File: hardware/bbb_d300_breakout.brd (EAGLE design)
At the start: 68 x 54.5 mm, 10 parts, among them SW1 JTP1236, X1 STEPCRAFT, X2 RJ45, X3 RJ45

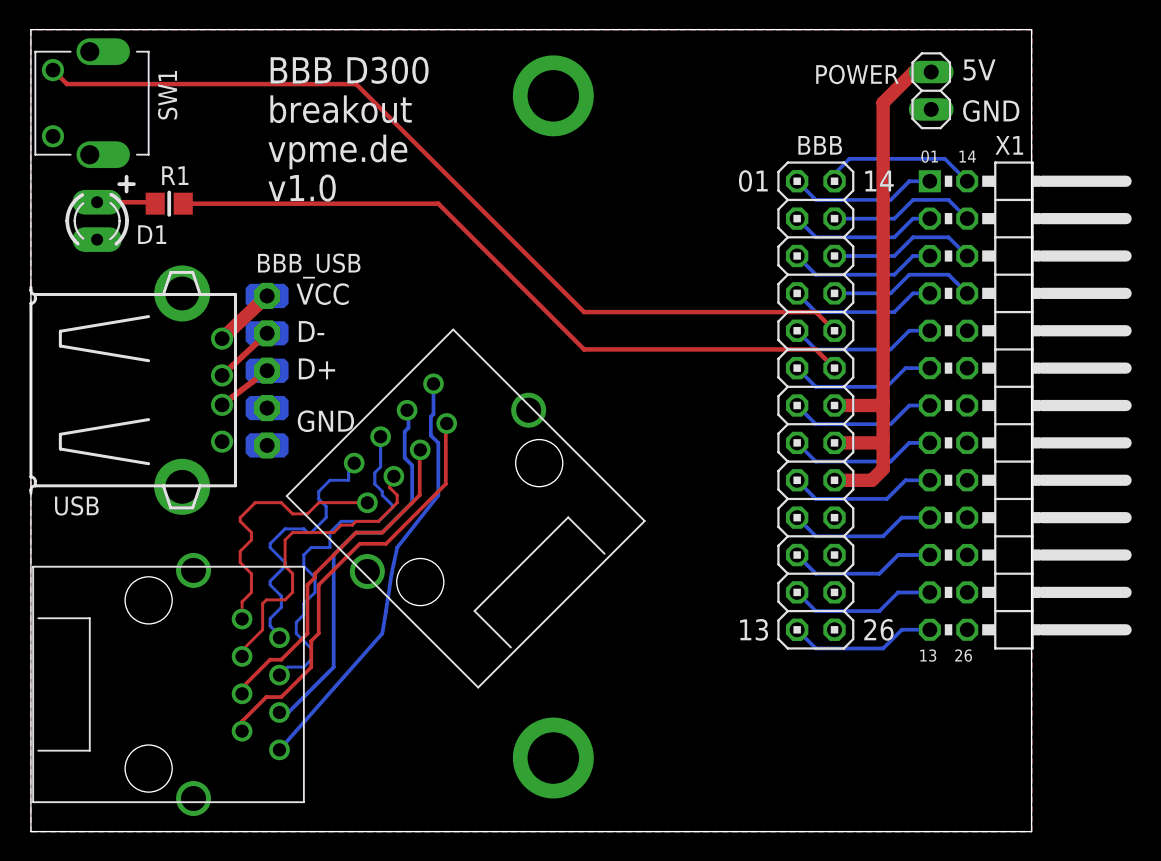
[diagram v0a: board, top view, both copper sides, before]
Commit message: swap USB and ETH position
Signed-off-by: Vladimir Pantelic <vladimir@pantelic.net>
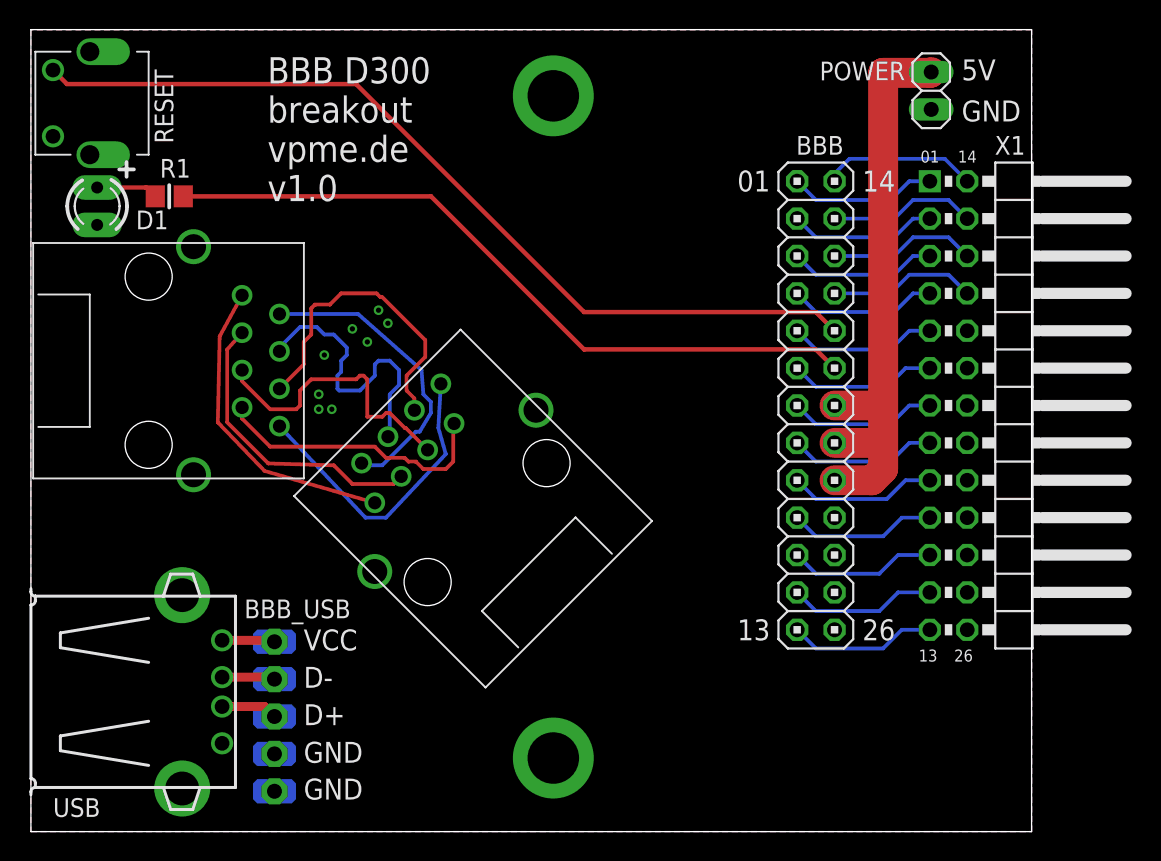
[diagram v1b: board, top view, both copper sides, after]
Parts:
- moved BBB_USB 23.5 mm to (16.6, 7.82)
- moved X2 22.0 mm to (8.00, 32.0)
- moved USB 20.5 mm to (0.00, 9.50)
- moved D1 1.00 mm to (4.50, 42.5)
- moved R1 0.50 mm to (9.40, 43.2)
- moved X3 0.50 mm to (31.0, 21.0)
- renumbered SW1 to RESET
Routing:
- net E7: track 28.3 -> 19.4 mm
- net E8: track 28.9 -> 20.7 mm
- net E4: track 24.5 -> 19.7 mm
- net E6: track 26.0 -> 21.4 mm
- net E1: track 17.8 -> 21.4 mm
- net E5: track 23.1 -> 19.5 mm
- net E2: track 18.5 -> 20.7 mm
- net 5V: track 39.5 -> 40.6 mm
- net E3: track 21.1 -> 20.2 mm
- net VBUS: track 4.22 -> 3.60 mm
- net DM: track 4.19 -> 3.62 mm
